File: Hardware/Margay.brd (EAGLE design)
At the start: 50.2 x 30.4 mm, 74 parts, among them IC1 ATMEGA644M, J7 CONN_6SCREW_2.54, Q2 DMG3404, Q3 2N7002, Q4 FDN360P, U1 TPS7A0533DBV, U2 FT231X-Q, U3 TPL5010DDC, U4 TLV3691DPF

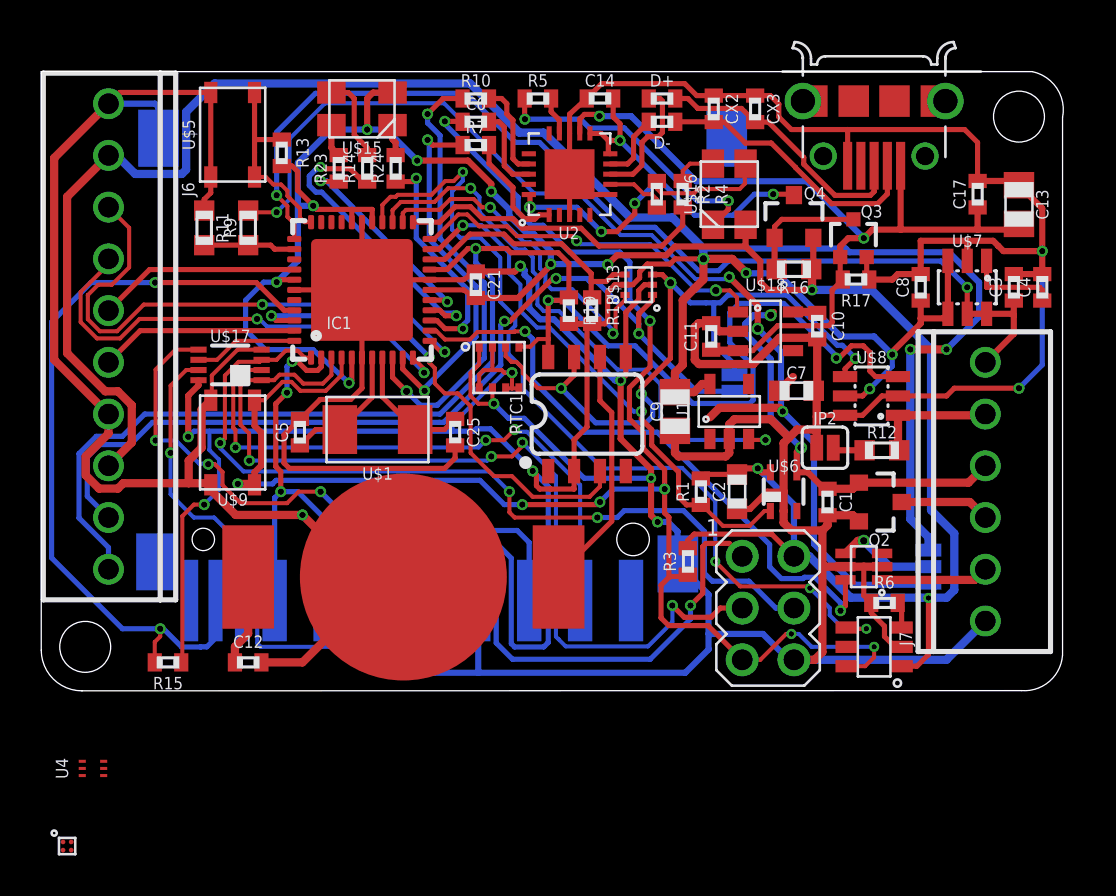
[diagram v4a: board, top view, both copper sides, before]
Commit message: improvements to aux power switch, layout complete
Completed layout of new aux power switch topology
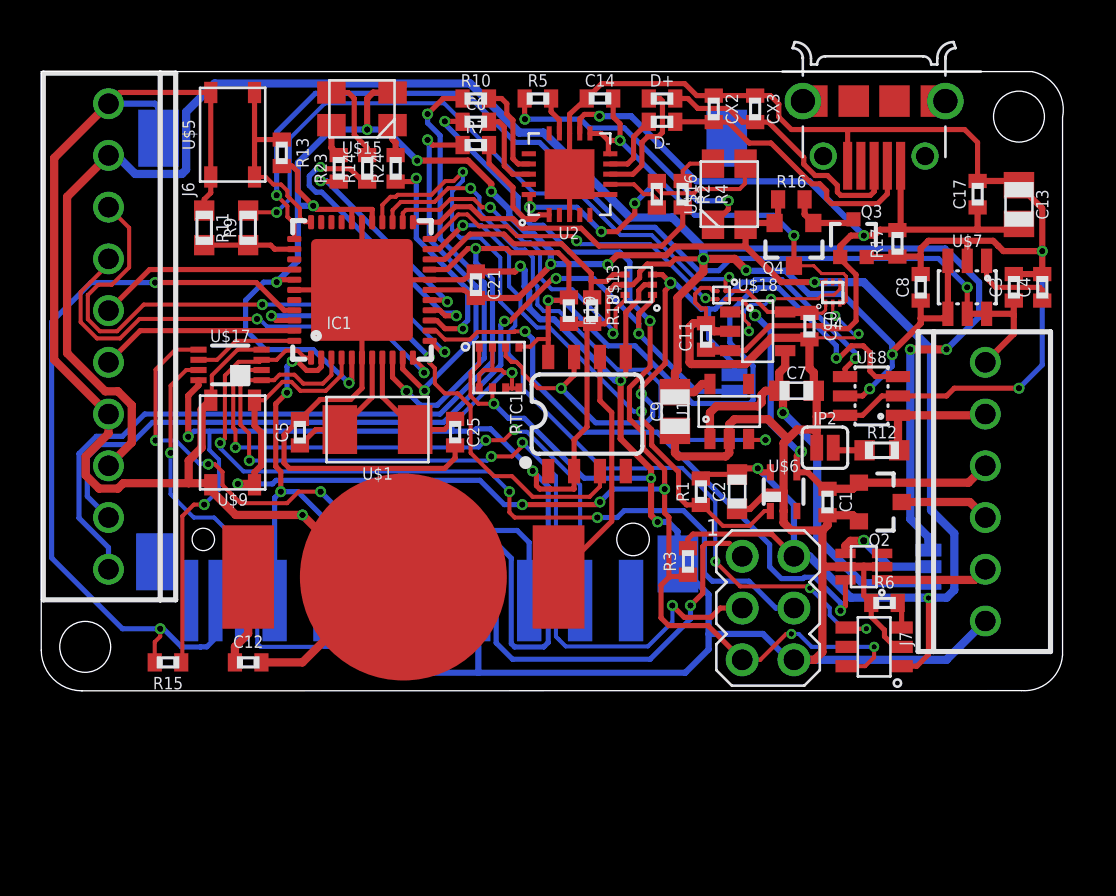
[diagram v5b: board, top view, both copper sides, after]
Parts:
- R16: device bschulz_passives:R0603 -> bschulz:R0402
- moved U4 43.2 mm to (38.9, 19.6), turned to 90 degrees
- moved U$4 42.0 mm to (33.4, 19.4), turned to 270 degrees
- moved R16 3.43 mm to (36.8, 24.1), turned to 0 degrees
- moved R17 2.70 mm to (42.0, 22.0), turned to 90 degrees
- moved Q4 1.27 mm to (37.0, 22.0), turned to 180 degrees
- moved C10 0.38 mm to (37.7, 17.9)
- moved U$18 0.38 mm to (35.2, 17.7)
- moved C11 0.25 mm to (32.6, 17.4)
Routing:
- net VMAIN: track 1.07 -> 22.0 mm, vias 0 -> 1
- net VBAT_SW: track 57.8 -> 37.8 mm, vias 4 -> 2
- net N$14: track 0.00 -> 8.23 mm, vias 0 -> 2
- net GND: track 323.4 -> 329.7 mm, vias 8 -> 10
- net 3V3_FTDI: track 24.1 -> 29.7 mm
- net N$6: track 6.16 -> 3.38 mm
- net VBAT_SW_CTRL: track 17.9 -> 16.3 mm
- net VUSB: track 41.3 -> 42.8 mm
- net SCL: track 77.1 -> 78.1 mm
- net SDA_OB: track 35.5 -> 36.4 mm
